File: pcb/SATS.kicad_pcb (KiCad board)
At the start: 2 copper layers, 108.5 x 103.4 mm, 34 parts, among them J1 Raspberry_Pi_2_3, J10 EXT_GPIO, J11 EXT_GPIO, J12 EXT_GPIO, J13 EXT_GPIO, J2 A00-432-262-450, J3 AudioJack4_SwitchTR1, J4 5V, J5 3.3V, J6 Card LED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

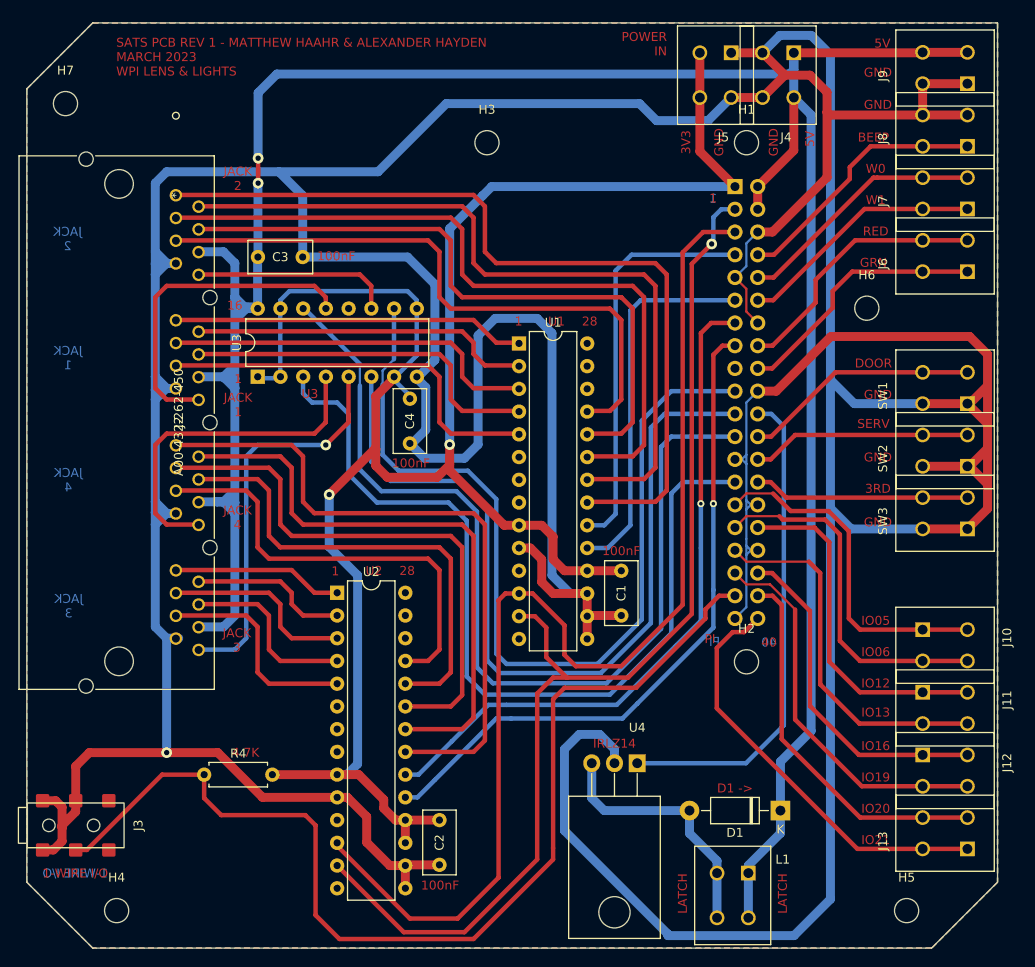
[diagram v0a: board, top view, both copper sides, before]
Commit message: Add Grounded Copper Fills to Row Breakout and Main Board
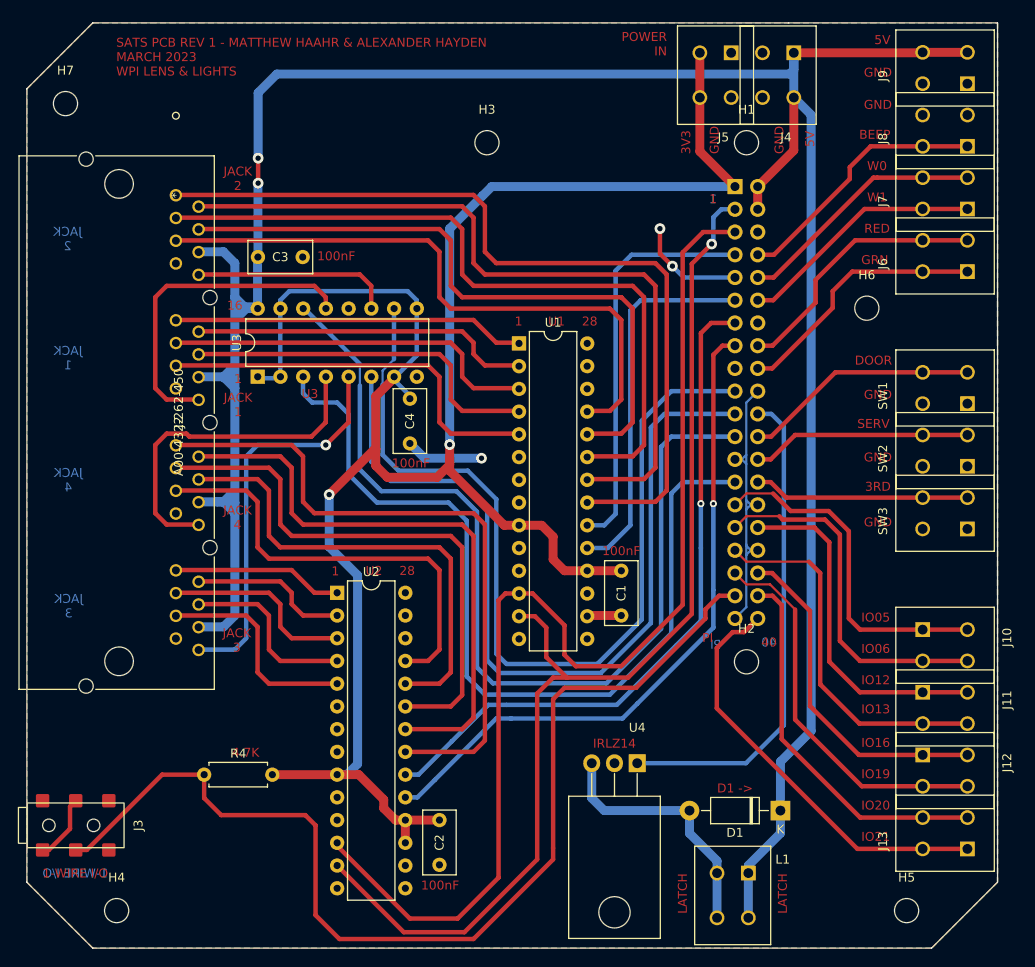
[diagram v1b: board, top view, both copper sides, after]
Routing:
- net Earth: track 715.7 -> 66.6 mm, vias 1 -> 3
- added copper zone on B.Cu, net Earth
- added copper zone on F.Cu, net Earth
- removed copper zone on B.Cu, net (none)
- removed copper zone on F.Cu, net (none)

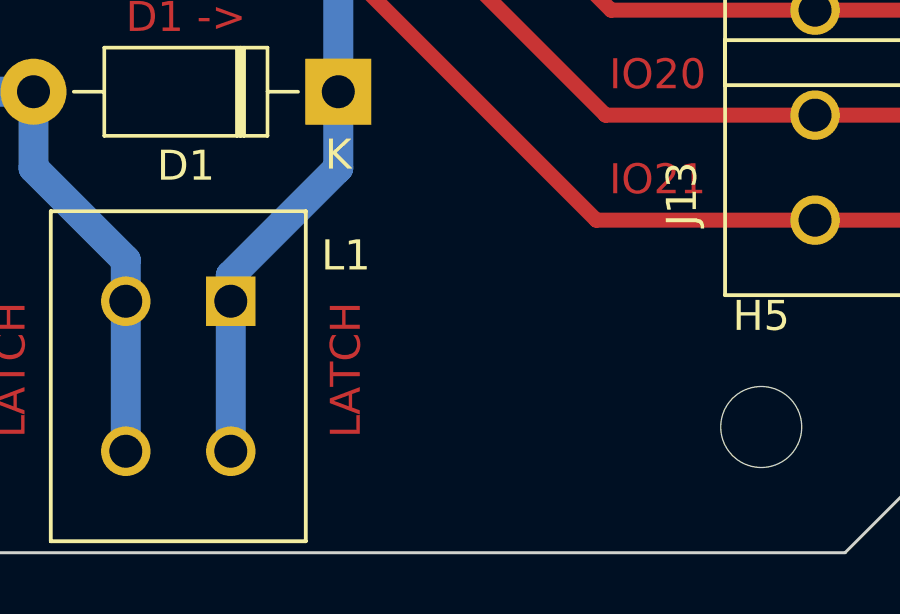
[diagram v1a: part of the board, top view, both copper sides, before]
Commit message: Add power cap for Latch
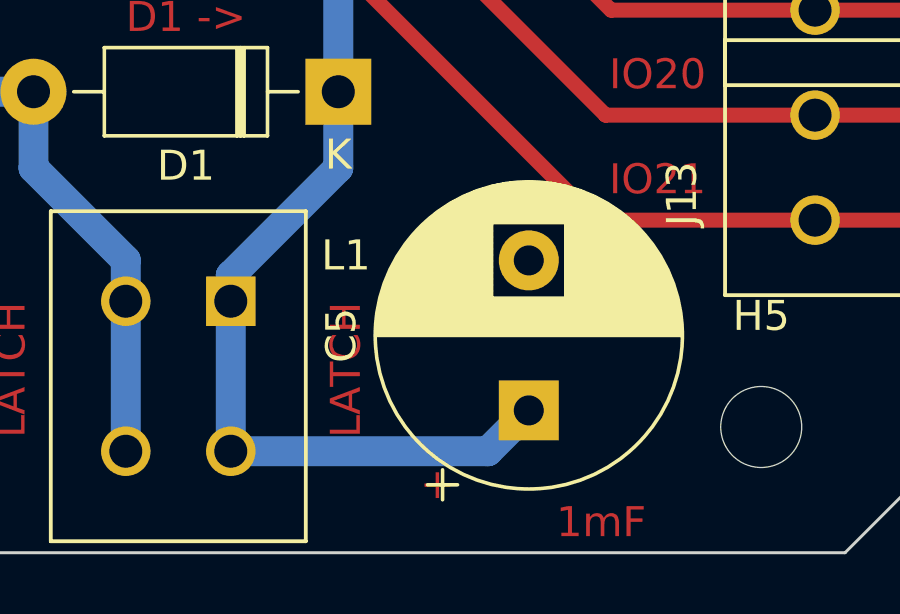
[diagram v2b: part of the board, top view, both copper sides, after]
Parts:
- added C5: 1mF, Capacitor_THT:CP_Radial_D10.0mm_P5.00mm, F.Cu at (140.2, 143.6)
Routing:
- net +5V: track 292.9 -> 303.4 mm
- net (no net): track 0.00 -> 0.76 mm
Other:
- board text added: "+"
- board text added: "1mF"

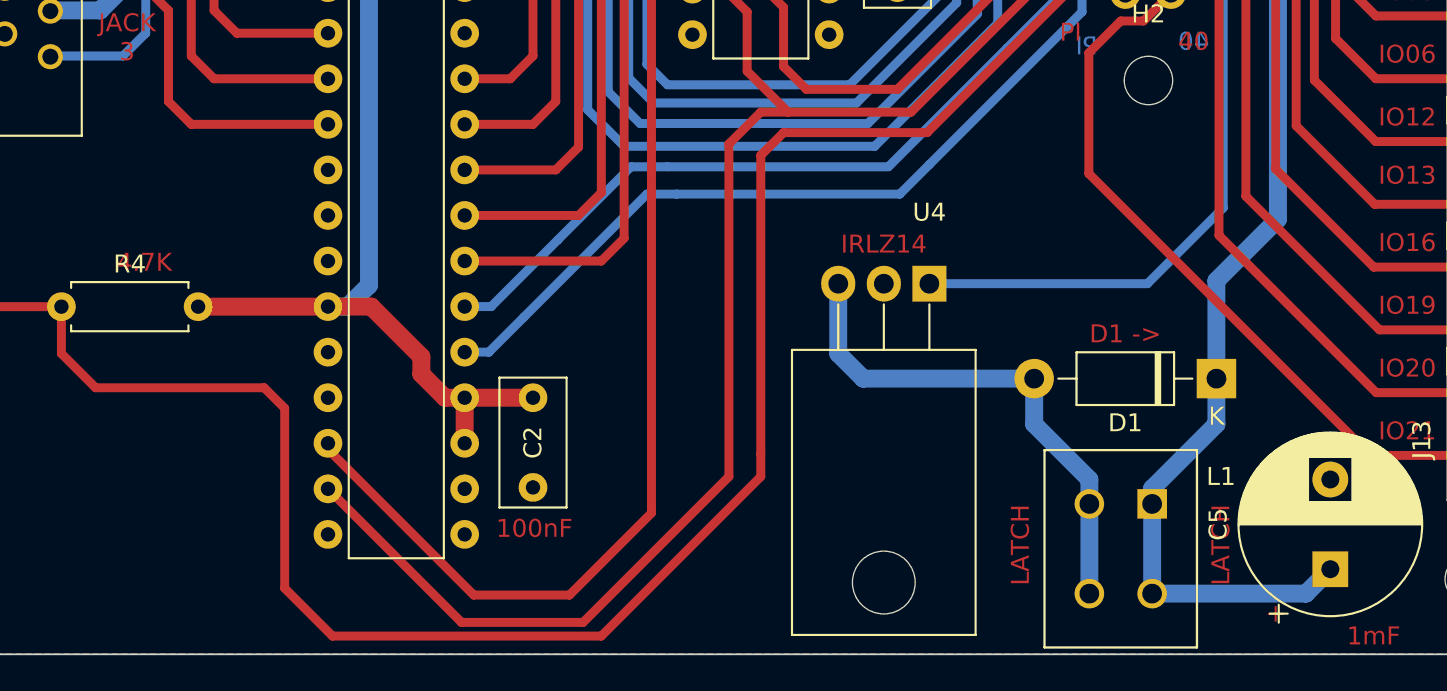
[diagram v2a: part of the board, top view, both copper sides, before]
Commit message: Update for better gerbers
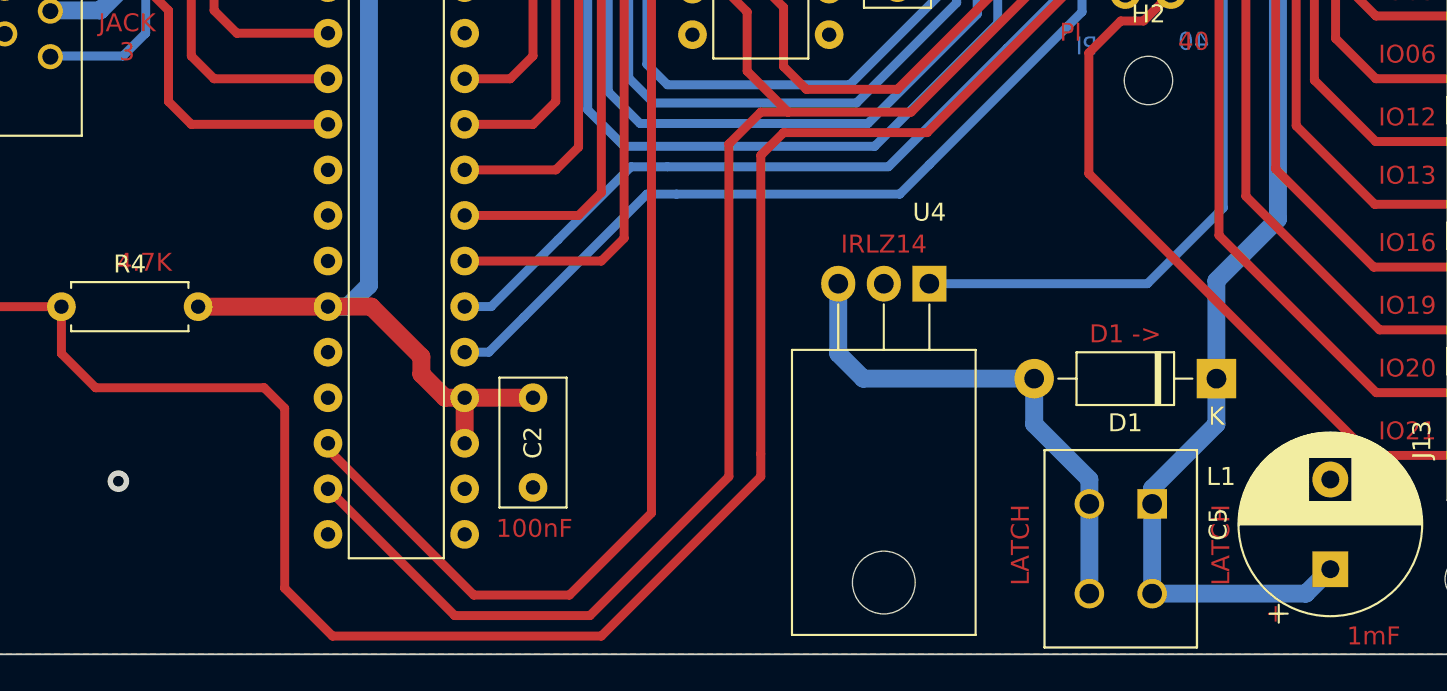
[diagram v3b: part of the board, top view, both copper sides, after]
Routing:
- net (no net): track 0.76 -> 0.00 mm
- net Earth: vias 3 -> 4
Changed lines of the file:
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@@
       (outputformat 1)
       (mirror false)
-      (drillshape 1)
+      (drillshape 0)
       (scaleselection 1)
-      (outputdirectory "")
+      (outputdirectory "Gerbers/")
     )
   )
@@
     )
   )
+  (gr_line (start 140.589 136.906) (end 139.827 136.906) (layer "F.Cu") (width 0.2))
   (gr_line (start 57.023 148.336) (end 49.657 140.97) (layer "Edge.Cuts") (width 0.1))
   (gr_line (start 158.115 140.97) (end 150.749 148.336) (layer "Edge.Cuts") (width 0.1))
@@
     (effects (font (size 1 1) (thickness 0.2)) (justify mirror))
   )
-  (segment (start 139.827 136.906) (end 140.589 136.906) (width 0.25) (layer "F.Cu") (net 0))
   (segment (start 102.997 101.092) (end 104.648 101.092) (width 1) (layer "F.Cu") (net 1))
   (segment (start 88.646 92.583) (end 88.646 94.4372) (width 1) (layer "F.Cu") (net 1))
@@
   (segment (start 54.483 132.505) (end 55.118 131.87) (width 0.5) (layer "F.Cu") (net 2))
   (segment (start 52.114 137.37) (end 54.483 135.001) (width 0.5) (layer "F.Cu") (net 2))
+  (via (at 72.644 138.684) (size 1.2) (drill 0.6) (layers "F.Cu" "B.Cu") (free) (net 2))
   (via (at 121.793 72.136) (size 1.2) (drill 0.6) (layers "F.Cu" "B.Cu") (free) (net 2))
   (via (at 100.457 93.599) (size 1.2) (drill 0.6) (layers "F.Cu" "B.Cu") (net 2))
@@
   (segment (start 126.774 139.953) (end 126.774 138.585) (width 1) (layer "B.Cu") (net 4))
   (segment (start 116.84 118.11) (end 123.952 110.998) (width 0.5) (layer "F.Cu") (net 5))
-  (segment (start 108.458 118.11) (end 109.982 118.11) (width 0.5) (layer "F.Cu") (net 5))
-  (segment (start 98.552 146.558) (end 106.68 138.43) (width 0.5) (layer "F.Cu") (net 5))
+  (segment (start 109.982 118.11) (end 108.458 118.11) (width 0.5) (layer "F.Cu") (net 5))
+  (segment (start 106.68 138.43) (end 98.933 146.177) (width 0.5) (layer "F.Cu") (net 5))
+  (segment (start 98.933 146.177) (end 91.393 146.177) (width 0.5) (layer "F.Cu") (net 5))
   (segment (start 123.952 110.998) (end 123.952 71.882) (width 0.5) (layer "F.Cu") (net 5))
-  (segment (start 91.774 146.558) (end 98.552 146.558) (width 0.5) (layer "F.Cu") (net 5))
   (segment (start 107.696 115.824) (end 107.696 112.522) (width 0.5) (layer "F.Cu") (net 5))
   (segment (start 109.982 118.11) (end 107.696 115.824) (width 0.5) (layer "F.Cu") (net 5))
   (segment (start 109.982 118.11) (end 116.84 118.11) (width 0.5) (layer "F.Cu") (net 5))
-  (segment (start 84.328 139.112) (end 91.774 146.558) (width 0.5) (layer "F.Cu") (net 5))
+  (segment (start 91.393 146.177) (end 84.328 139.112) (width 0.5) (layer "F.Cu") (net 5))
+  (segment (start 106.68 119.888) (end 106.68 138.43) (width 0.5) (layer "F.Cu") (net 5))
+  (segment (start 108.458 118.11) (end 106.68 119.888) (width 0.5) (layer "F.Cu") (net 5))
   (segment (start 106.426 111.252) (end 104.648 111.252) (width 0.5) (layer "F.Cu") (net 5))
   (segment (start 123.952 71.882) (end 126.1745 69.6595) (width 0.5) (layer "F.Cu") (net 5))
-  (segment (start 106.68 119.888) (end 108.458 118.11) (width 0.5) (layer "F.Cu") (net 5))
   (segment (start 107.696 112.522) (end 106.426 111.252) (width 0.5) (layer "F.Cu") (net 5))
-  (segment (start 106.68 138.43) (end 106.68 119.888) (width 0.5) (layer "F.Cu") (net 5))
   (via (at 126.1745 69.6595) (size 1.2) (drill 0.6) (layers "F.Cu" "B.Cu") (net 5))
   (segment (start 128.778 65.786) (end 127.254 65.786) (width 0.5) (layer "B.Cu") (net 5))

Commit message: Rev 3 Complete
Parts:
- removed R4: 4.7k, Resistor_THT:R_Axial_DIN0207_L6.3mm_D2.5mm_P7.62mm_Horizontal
- added R1: 4.7k, Resistor_THT:R_Axial_DIN0207_L6.3mm_D2.5mm_P7.62mm_Horizontal, F.Cu at (69.5, 129.0)
- added R2: 10, Resistor_THT:R_Axial_DIN0207_L6.3mm_D2.5mm_P7.62mm_Horizontal, F.Cu at (121.4, 133.5)
- moved U4 1.27 mm to (116.6, 127.7)
- moved D1 1.02 mm to (134.7, 133.5)
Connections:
- L1 pad 3: Net-(D1-Pad2) -> Net-(L1-Pad3)
- L1 pad 4: Net-(D1-Pad2) -> Net-(L1-Pad3)
- U4 pad 3: Net-(D1-Pad2) -> Net-(L1-Pad3)
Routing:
- net Earth: track 66.6 -> 97.3 mm
- net Net-(L1-Pad3): track 0.00 -> 27.9 mm
- net Net-(D1-Pad2): track 28.7 -> 3.17 mm
- net Latch: track 55.0 -> 56.3 mm
- net +5V: vias 2 -> 0
- removed copper zone on F.Cu, net Earth
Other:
- board text added: "10"
- board text added: "SATS PCB REV 3 - MATTHEW HAAHR & ALEXANDER HAYDEN MARCH 2023 WPI LENS & LIGHTS"
- board text added: "TOUCH"
- board text removed: "+"
- board text removed: "1mF"
- board text removed: "D1 ->"
- board text removed: "IO05"
- board text removed: "SATS PCB REV 1 - MATTHEW HAAHR & ALEXANDER HAYDEN MARCH 2023 WPI LENS & LIGHTS"
- board text removed: "U1"
- board text removed: "U2"
- board text removed: "U3"

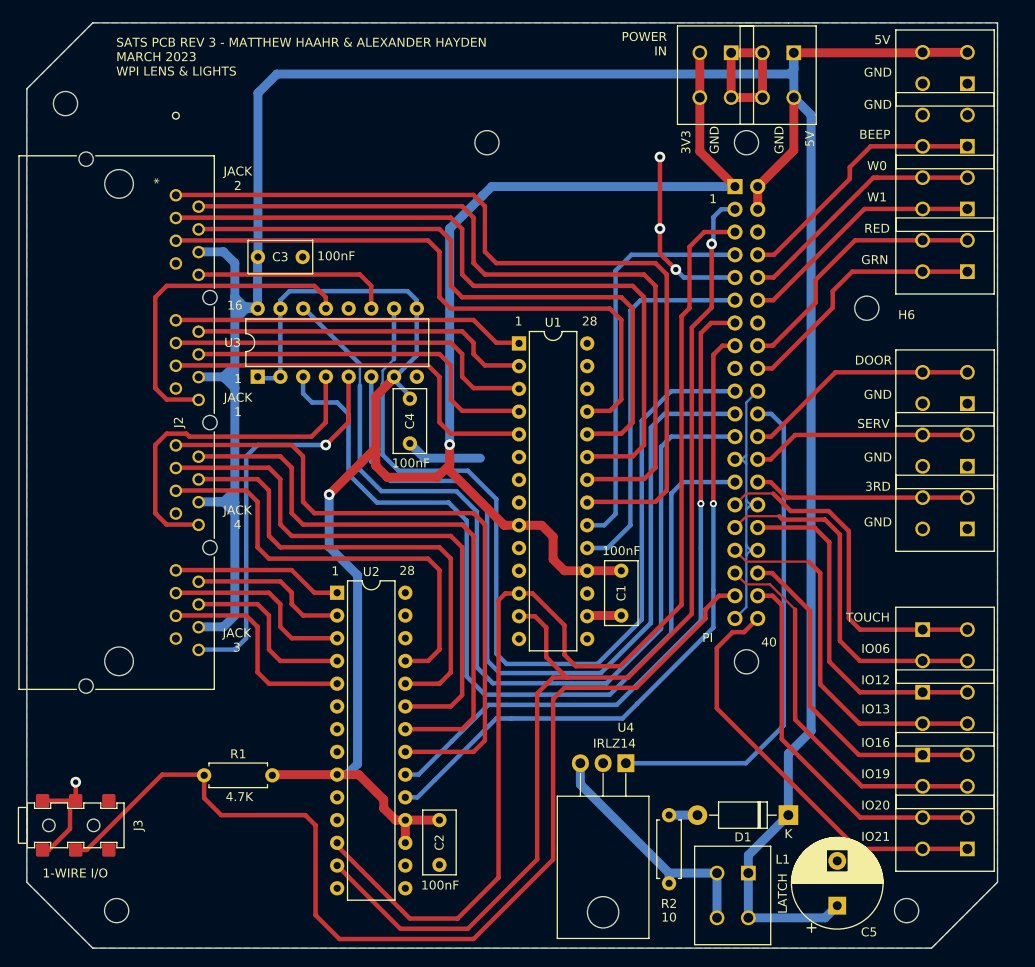
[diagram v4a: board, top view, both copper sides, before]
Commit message: Fix resistor, redate
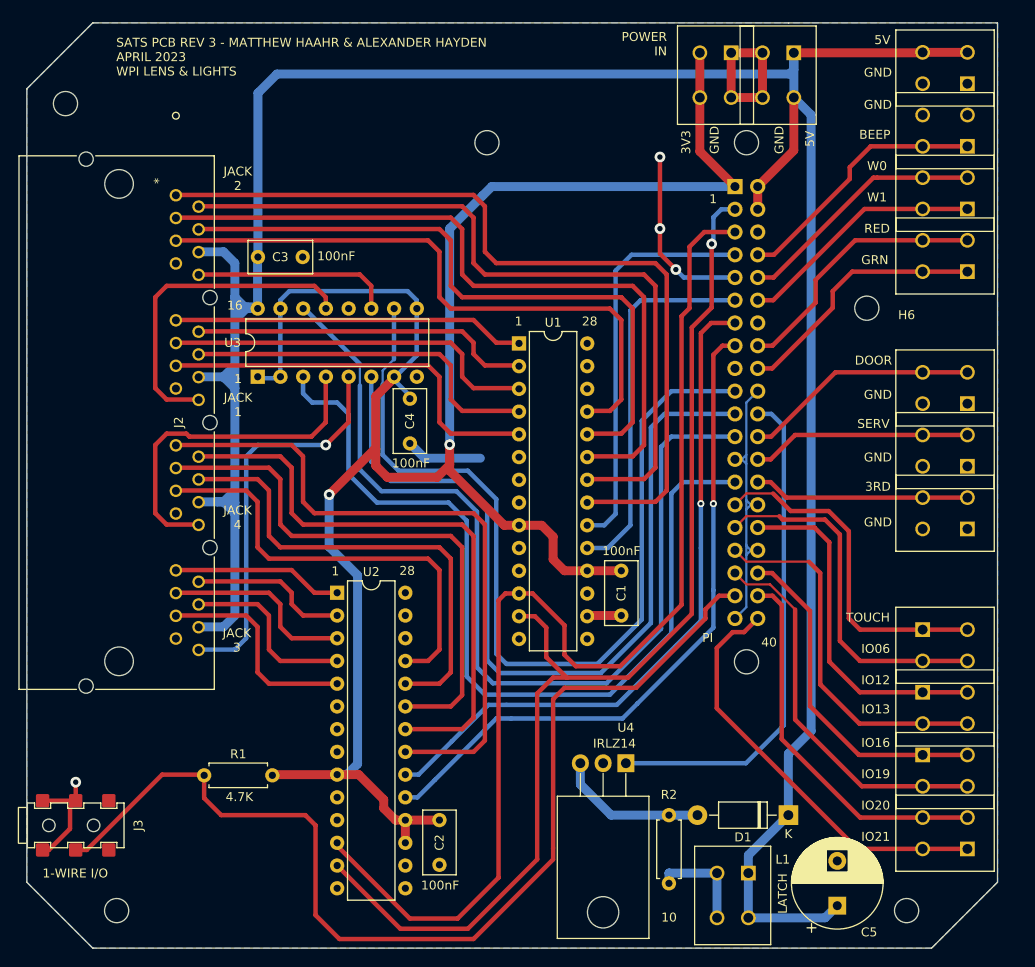
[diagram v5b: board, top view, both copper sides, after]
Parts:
- moved R2 7.62 mm to (121.4, 141.1), turned to 90 degrees
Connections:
- D1 pad 2: Net-(D1-Pad2) -> Net-(D1-A)
- L1 pad 3: Net-(L1-Pad3) -> Net-(L1-2-Pad3)
- L1 pad 4: Net-(L1-Pad3) -> Net-(L1-2-Pad3)
- R2 pad 1: Net-(D1-Pad2) -> Net-(L1-2-Pad3)
- R2 pad 2: Net-(L1-Pad3) -> Net-(D1-A)
- U4 pad 3: Net-(L1-Pad3) -> Net-(D1-A)
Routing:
- net Net-(L1-Pad3): track 27.9 -> 0.00 mm
- net Net-(D1-A): track 0.00 -> 16.9 mm
- net Net-(L1-2-Pad3): track 0.00 -> 11.5 mm
- net Net-(D1-Pad2): track 3.17 -> 0.00 mm
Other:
- board text added: "SATS PCB REV 3 - MATTHEW HAAHR & ALEXANDER HAYDEN APRIL 2023 WPI LENS & LIGHTS"
- board text removed: "SATS PCB REV 3 - MATTHEW HAAHR & ALEXANDER HAYDEN MARCH 2023 WPI LENS & LIGHTS"

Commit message: Reev 3
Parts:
- removed H7: MountingHole, MountingHole:MountingHole_2.7mm_M2.5
- added J14: EXT_GPIO, TerminalConn:PHOENIX_1862042, F.Cu at (152.2, 136.8)
- J10: value EXT_GPIO -> SENSE
- J11: value EXT_GPIO -> SENSE Power
- moved H6 92.4 mm to (53.9, 54.0)
- moved J10 9.50 mm to (152.2, 105.0)
- moved J11 8.75 mm to (152.2, 112.8)
- moved J12 5.75 mm to (152.2, 122.8)
- moved J13 5.75 mm to (152.2, 129.8), turned to -90 degrees
- moved SW1 4.75 mm to (152.2, 81.0)
- moved SW2 4.75 mm to (152.2, 88.0)
- moved SW3 4.75 mm to (152.2, 95.0)
- moved C5 1.48 mm to (138.9, 144.4)
- moved H5 0.67 mm to (147.8, 144.8)
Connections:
- net EXT_GPIO5 renamed TOUCH
- net EXT_GPIO6 renamed PHOTO
- J11 pad 1: EXT_GPIO12 -> Earth
- J11 pad 2: EXT_GPIO12 -> Earth
- J11 pad 3: EXT_GPIO13 -> +5V
- J11 pad 4: EXT_GPIO13 -> +5V
- J12 pad 1: EXT_GPIO16 -> EXT_GPIO12
- J12 pad 2: EXT_GPIO16 -> EXT_GPIO12
- J12 pad 3: EXT_GPIO19 -> EXT_GPIO13
- J12 pad 4: EXT_GPIO19 -> EXT_GPIO13
- J13 pad 1: EXT_GPIO21 -> EXT_GPIO16
- J13 pad 2: EXT_GPIO21 -> EXT_GPIO16
- J13 pad 3: EXT_GPIO20 -> EXT_GPIO19
- J13 pad 4: EXT_GPIO20 -> EXT_GPIO19
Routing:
- net +5V: track 303.4 -> 320.1 mm
- net PHOTO: track 40.2 -> 29.2 mm
- net TOUCH: track 38.5 -> 28.8 mm
- net Serv Door: track 24.6 -> 26.5 mm
- net Main Door: track 26.4 -> 28.4 mm
- net Third Reed: track 24.2 -> 24.7 mm
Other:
- board text added: "PHOTO"
- board text removed: "IO06"
